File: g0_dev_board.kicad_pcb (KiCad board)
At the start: 4 copper layers, 80 x 114 mm, 198 parts, among them J201 USB_B_Mini, J202 F103_SWD, J301 USB_B_Mini, J401 RJ45_Hanrun_HR911105A_Horizon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, J501 DM3AT-SF-PEJM5, J801 Uno_IOH, J802 Uno_IOL, J803 Uno_POWER, J804 Uno_ANALOG, J805 J_LA_L, J806 J_LA_R, Q201 MMBT3904, SW701 RESET, SW702 USER, U101 STM32G0B1CCT6, U201 USBLC6-2SC6, U202 AP7361C-33E, U203 STM32F103CBTx, U301 USBLC6-2SC6, U302 FT232RL, U401 W5500, U501 W25Q32JVSSIQ, U601 TMP100, U602 TMP100, Y101 32.768kHz CL7pF, Y201 8MHz, Y401 25MHz

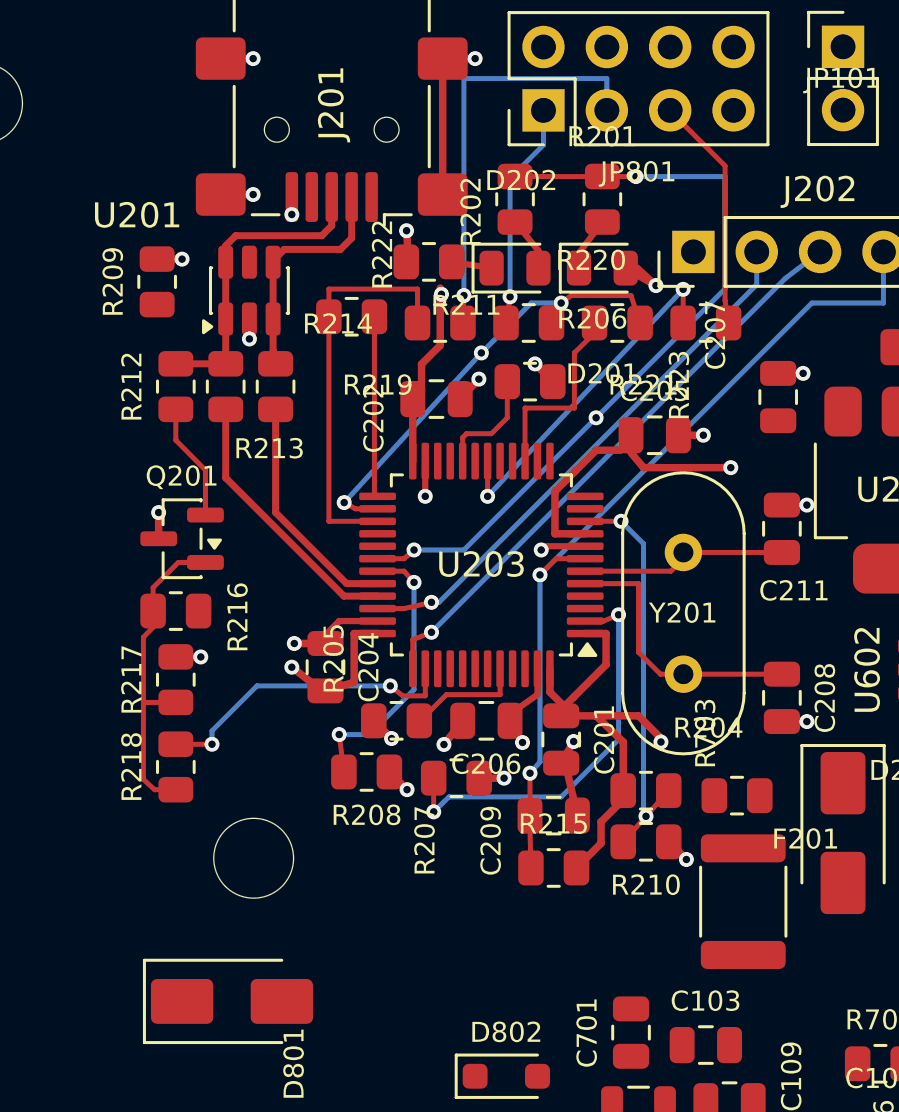
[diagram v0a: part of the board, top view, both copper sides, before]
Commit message: feat(pcb): route ST-Link VBUS and USB ID
VBUS_STL от J201 по B.Cu левой колонкой (x=112.9, 0.5 мм) вниз и к F201,
отводы к U201 (переходное 0.45/0.3 между линиями D+/D-) и к R216. ID от
J201.4 к R209 по B.Cu. GND R209 подключён к экрану разъёма по F.Cu вместо
переходного на пути VBUS. DRC: 0 ошибок, 388 неразведённых.
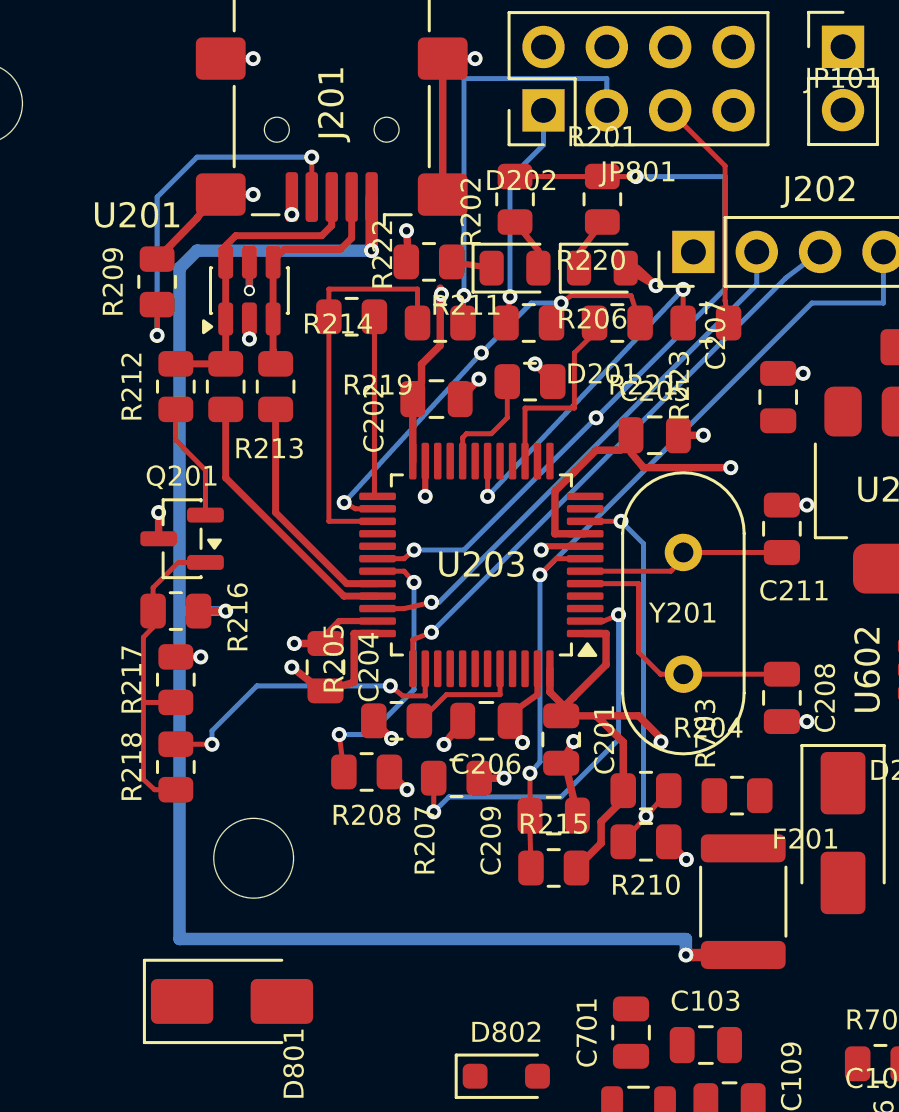
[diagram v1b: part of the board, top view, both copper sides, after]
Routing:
- net /st_link/VBUS_STL: track 0.00 -> 66.0 mm, vias 0 -> 4
- net Net-(J201-ID): track 0.00 -> 15.3 mm, vias 0 -> 2
- net GND: track 39.3 -> 41.0 mm, vias 24 -> 23
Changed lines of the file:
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@@
+	)
+	(segment
+		(start 113.6 45.6)
+		(end 113.9 45.2)
+		(width 0.3)
+		(layer "F.Cu")
+		(net "GND")
 	)
 	(segment
@@
 	)
 	(segment
+		(start 112 47.237)
+		(end 113.6 45.6)
+		(width 0.3)
+		(layer "F.Cu")
+		(net "GND")
+	)
+	(segment
 		(start 129.16 58.75)
 		(end 127.6 58.75)
@@
 	)
 	(segment
-		(start 112 47.237)
-		(end 113 47.24)
-		(width 0.3)
-		(layer "F.Cu")
-		(net "GND")
-	)
-	(segment
 		(start 127.25 64.7)
 		(end 126.4 65.3)
@@
 	)
 	(via
-		(at 113 47.24)
-		(size 0.6)
-		(drill 0.3)
-		(layers "F.Cu" "B.Cu")
-		(net "GND")
-	)
-	(via
 		(at 115.85 39.2)
 		(size 0.6)
@@
 	)
 	(segment
+		(start 118.2 44.75)
+		(end 118.2 43.15)
+		(width 0.2)
+		(layer "F.Cu")
+		(net "Net-(J201-ID)")
+	)
+	(segment
+		(start 112 50.3)
+		(end 112 49.062)
+		(width 0.2)
+		(layer "F.Cu")
+		(net "Net-(J201-ID)")
+	)
+	(via
+		(at 112 50.3)
+		(size 0.6)
+		(drill 0.3)
+		(layers "F.Cu" "B.Cu")
+		(net "Net-(J201-ID)")
+	)
+	(via
+		(at 118.2 43.15)
+		(size 0.6)
+		(drill 0.3)
+		(layers "F.Cu" "B.Cu")
+		(net "Net-(J201-ID)")
+	)
+	(segment
+		(start 118.2 43.15)
+		(end 113.6 43.15)
+		(width 0.2)
+		(layer "B.Cu")
+		(net "Net-(J201-ID)")
+	)
+	(segment
+		(start 113.6 43.15)
+		(end 112 44.75)
+		(width 0.2)
+		(layer "B.Cu")
+		(net "Net-(J201-ID)")
+	)
+	(segment
+		(start 112 44.75)
+		(end 112 50.3)
+		(width 0.2)
+		(layer "B.Cu")
+		(net "Net-(J201-ID)")
+	)
+	(segment
 		(start 119 44.75)
 		(end 119 45.9)
@@
 	)
 	(segment
+		(start 133.199999 75.14)
+		(end 135.5 75.138)
+		(width 0.5)
+		(layer "F.Cu")
+		(net "/st_link/VBUS_STL")
+	)
+	(segment
+		(start 113.66 61.35)
+		(end 114.75 61.35)
+		(width 0.3)
+		(layer "F.Cu")
+		(net "/st_link/VBUS_STL")
+	)
+	(segment
+		(start 115.7 47.362)
+		(end 115.7 48.5)
+		(width 0.25)
+		(layer "F.Cu")
+		(net "/st_link/VBUS_STL")
+	)
+	(segment
+		(start 120.6 44.75)
+		(end 120.6 46.9)
+		(width 0.5)
+		(layer "F.Cu")
+		(net "/st_link/VBUS_STL")
+	)
+	(via
+		(at 115.7 48.5)
+		(size 0.45)
+		(drill 0.3)
+		(layers "F.Cu" "B.Cu")
+		(net "/st_link/VBUS_STL")
+	)
+	(via
+		(at 114.75 61.35)
+		(size 0.6)
+		(drill 0.3)
+		(layers "F.Cu" "B.Cu")
+		(net "/st_link/VBUS_STL")
+	)
+	(via
+		(at 133.199999 75.14)
+		(size 0.6)
+		(drill 0.3)
+		(layers "F.Cu" "B.Cu")
+		(net "/st_link/VBUS_STL")
+	)
+	(via
+		(at 120.6 46.9)
+		(size 0.6)
+		(drill 0.3)
+		(layers "F.Cu" "B.Cu")
+		(net "/st_link/VBUS_STL")
+	)
+	(segment
+		(start 113.6 46.9)
+		(end 112.9 47.6)
+		(width 0.5)
+		(layer "B.Cu")
+		(net "/st_link/VBUS_STL")
+	)
+	(segment
+		(start 114.75 61.35)
+		(end 112.9 61.35)
+		(width 0.4)
+		(layer "B.Cu")
+		(net "/st_link/VBUS_STL")
+	)
+	(segment
+		(start 112.9 47.6)
+		(end 112.9 74.5)
+		(width 0.5)
+		(layer "B.Cu")
+		(net "/st_link/VBUS_STL")
+	)
+	(segment
+		(start 115.7 48.5)
+		(end 115.7 46.9)
+		(width 0.3)
+		(layer "B.Cu")
+		(net "/st_link/VBUS_STL")
+	)
+	(segment
+		(start 112.9 74.5)
+		(end 133.199999 74.5)
+		(width 0.5)
+		(layer "B.Cu")
+		(net "/st_link/VBUS_STL")
+	)
+	(segment
+		(start 120.6 46.9)
+		(end 113.6 46.9)
+		(width 0.5)
+		(layer "B.Cu")
+		(net "/st_link/VBUS_STL")
+	)
+	(segment
+		(start 133.199999 74.5)
+		(end 133.199999 75.14)
+		(width 0.5)
+		(layer "B.Cu")
+		(net "/st_link/VBUS_STL")
+	)
+	(segment

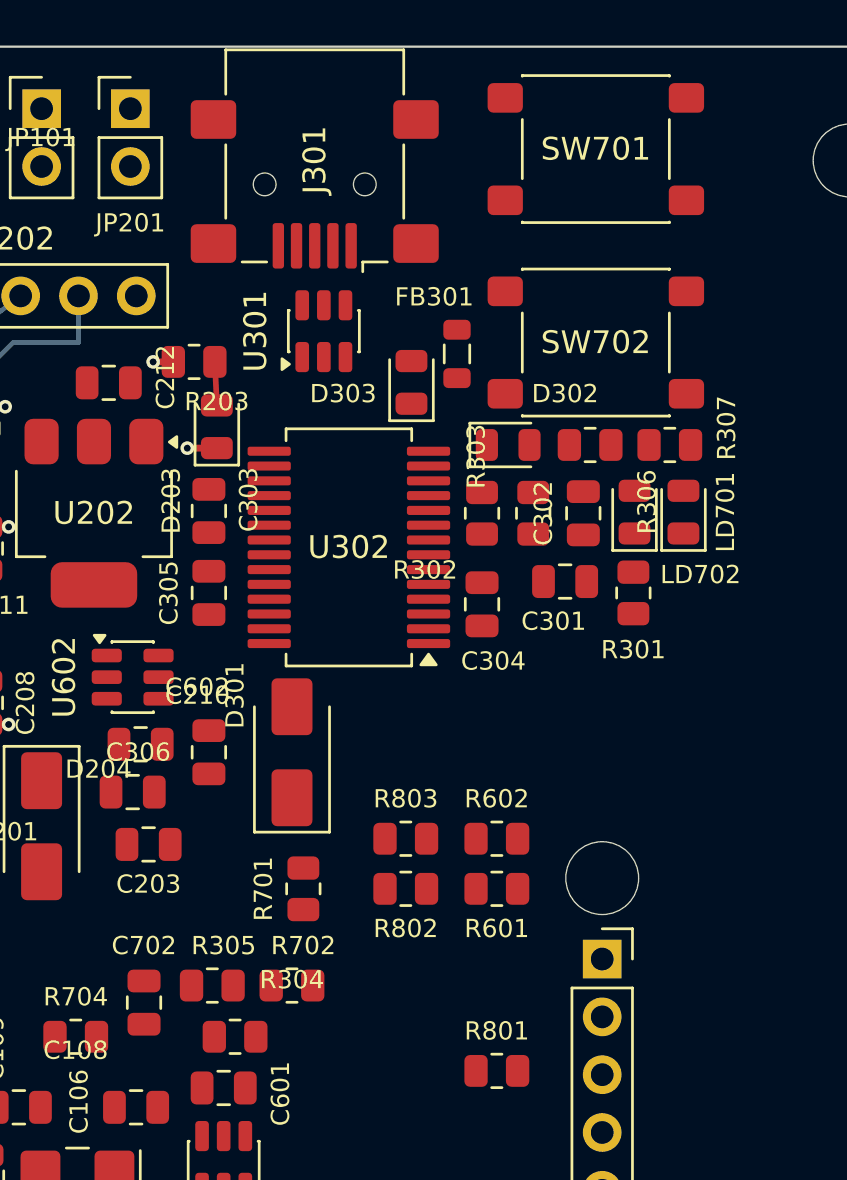
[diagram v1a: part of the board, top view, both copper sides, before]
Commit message: feat(pcb): route FT232RL block
USB-пара J301 -> USBLC6 -> FT232 (D+ по F.Cu, D- одним переходом на B.Cu
из-за зеркального порядка выводов), VBUS_FT к ESD, FB301 и делителю RESET,
линия FB301 -> D301 по B.Cu. Сигналы RX/TX LED выведены по F.Cu из-под
корпуса через торец, RXD/TXD — вниз по B.Cu к R304/R305, RESET по B.Cu.
Экран J301 связан и выведен на R301/C301. D203 сдвинута, R302/C302/C303
повёрнуты. DRC: 0 ошибок, 342 неразведённых.
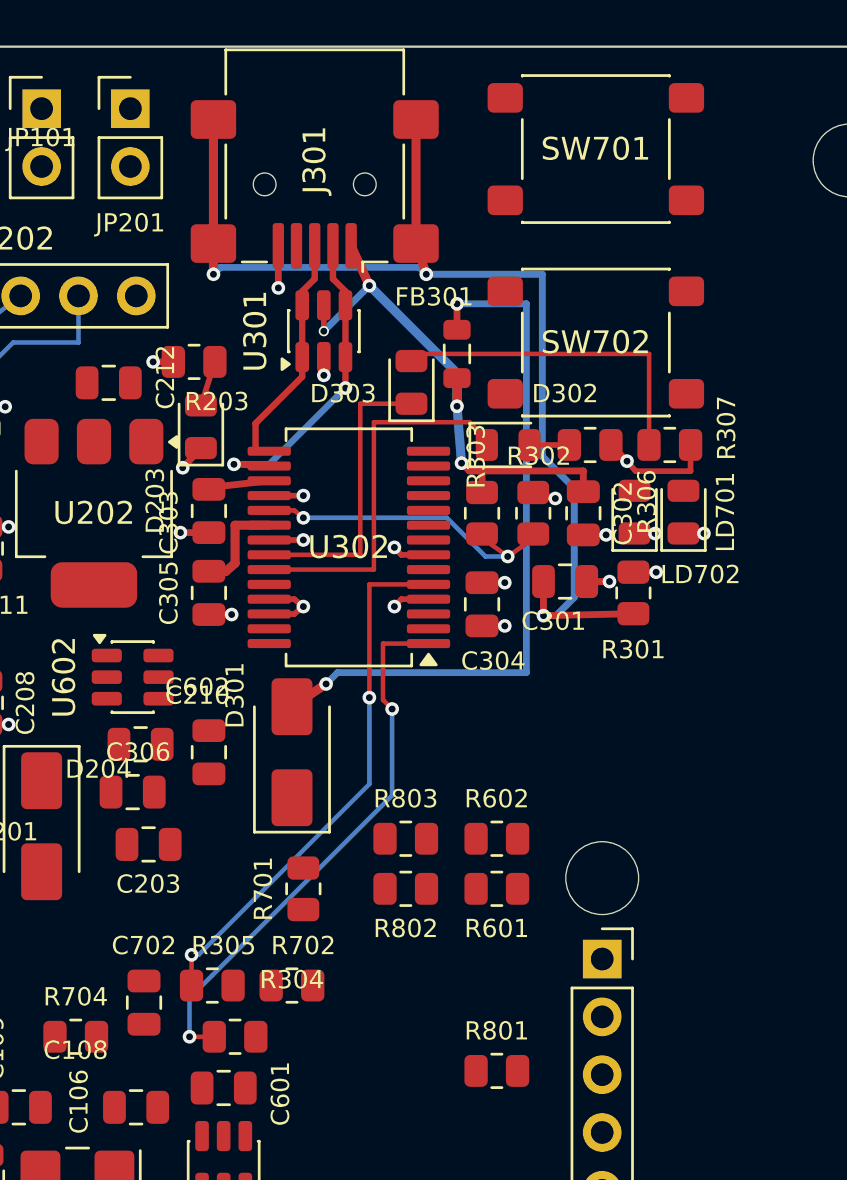
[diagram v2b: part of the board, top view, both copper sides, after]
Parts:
- moved D203 0.70 mm to (146.5, 52.7)
- turned C302 to -90 degrees
- turned C303 to -90 degrees
- turned R302 to -90 degrees
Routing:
- net /ft232rl/FT_SHIELD: track 0.00 -> 50.3 mm, vias 0 -> 3
- net Net-(D301-A): track 0.00 -> 31.2 mm, vias 0 -> 2
- net Net-(U302-TXD): track 0.00 -> 24.2 mm, vias 0 -> 2
- net /ft232rl/VBUS_FT: track 0.00 -> 23.9 mm, vias 0 -> 4
- net Net-(U302-RXD): track 0.00 -> 23.6 mm, vias 0 -> 2
- net GND: track 41.0 -> 60.5 mm, vias 23 -> 38
- net /ft232rl/FT_TXLED: track 0.00 -> 16.6 mm
- net Net-(D303-A): track 0.00 -> 14.5 mm
- net /ft232rl/FT_D-: track 0.00 -> 14.3 mm, vias 0 -> 2
- net /ft232rl/FT_RESET_N: track 0.00 -> 14.1 mm, vias 0 -> 2
- net /ft232rl/FT_RXLED: track 0.00 -> 12.9 mm
- net /ft232rl/FT_D+: track 0.00 -> 10.7 mm
- net +3.3V: track 0.89 -> 8.68 mm, vias 1 -> 4
- net +5V: track 0.00 -> 4.46 mm
- net /ft232rl/FT_3V3: track 0.00 -> 2.68 mm
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
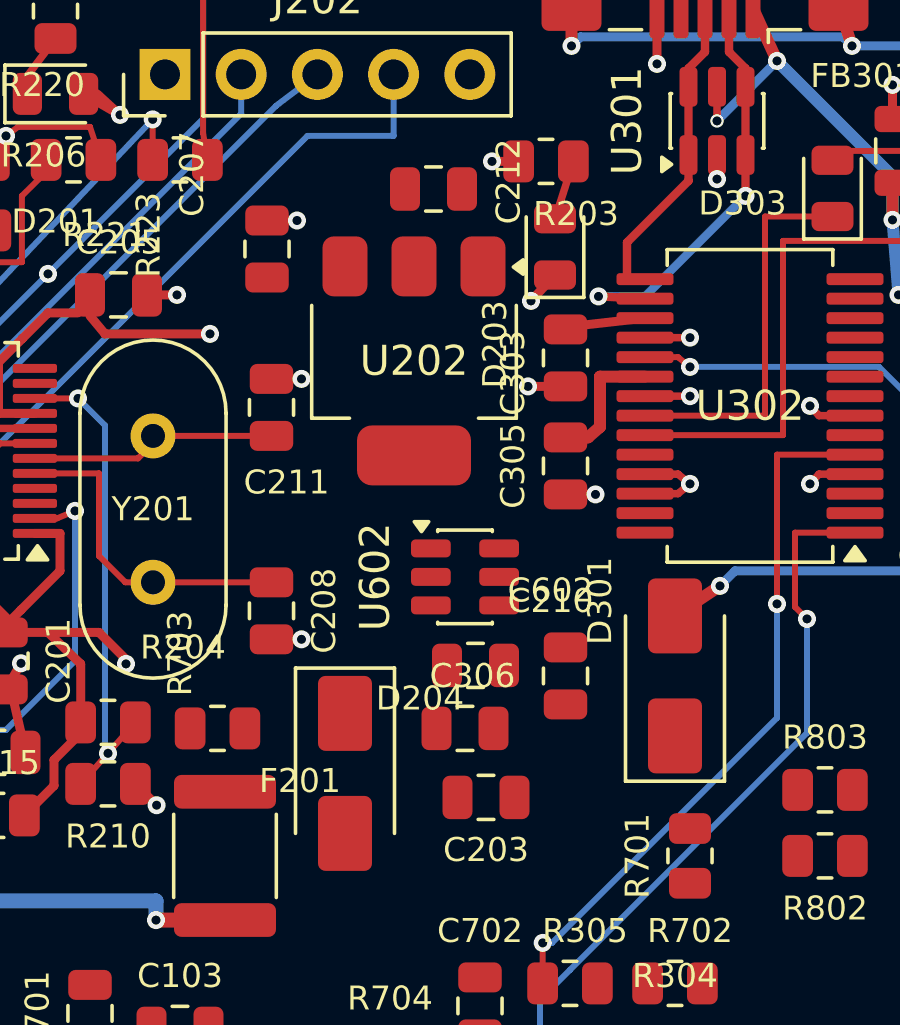
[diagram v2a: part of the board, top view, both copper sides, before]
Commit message: feat(pcb): route LDO input/output and +5V cluster
F201 -> D204 (0.8 мм), +5V: D204/C306/C203 и D301/C210 связаны с входом
LDO и C305/FT232 через B.Cu (прямой коридор по F.Cu перекрыт развязкой
FT232). Выход LDO +3.3V двумя переходными в плоскость In2, таб LDO на GND
шестью переходными. DRC: 0 ошибок, 329 неразведённых.
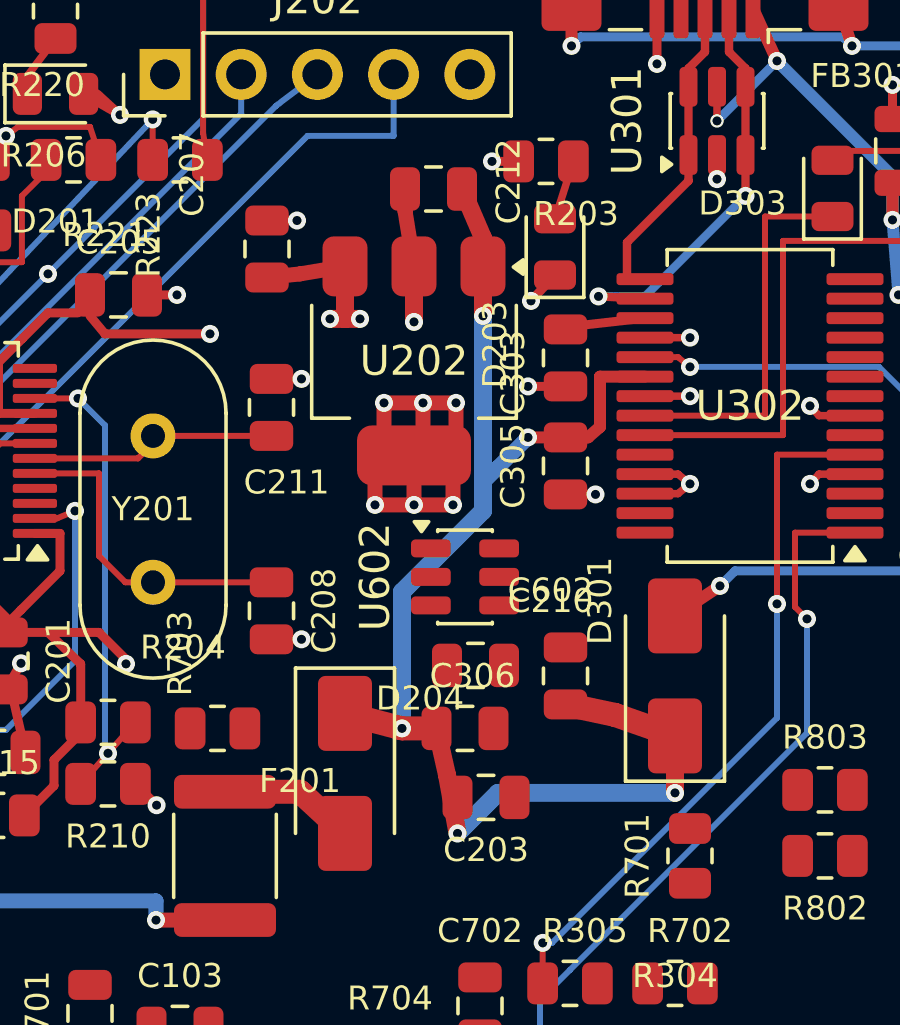
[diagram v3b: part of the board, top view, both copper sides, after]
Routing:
- net +5V: track 4.46 -> 47.3 mm, vias 0 -> 5
- net GND: track 60.5 -> 74.5 mm, vias 38 -> 45
- net +3.3V: track 8.68 -> 14.1 mm, vias 4 -> 6
- net Net-(D204-A): track 0.00 -> 4.54 mm
